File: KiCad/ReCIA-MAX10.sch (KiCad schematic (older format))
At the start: 30 parts, among them J1 Conn_02x03_Odd_Even, U1 AMS1117-3.3, U2 SN74CBT16210, U3 SN74CBT16210, U4 10M02SCU169, U5 8520_DIP_SOCKET, X1 Oscillator_3.2x2.5mm-28.6363M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

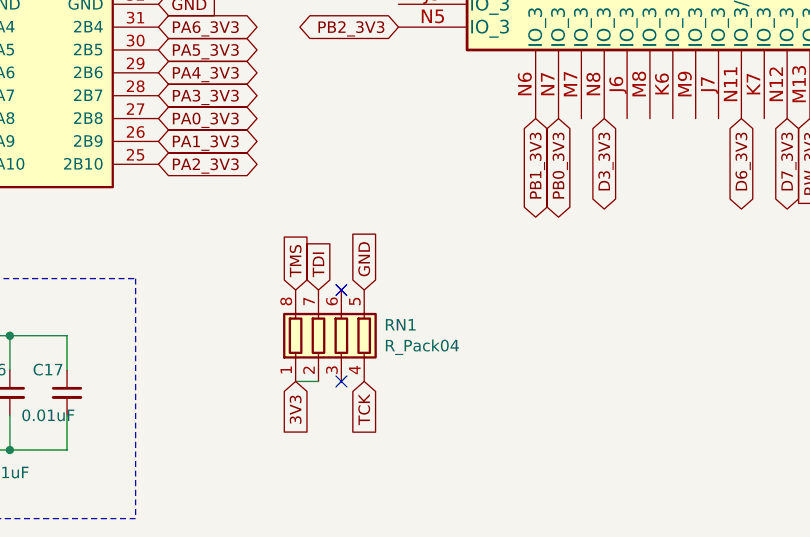
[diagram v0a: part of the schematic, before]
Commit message: Add 10k resistor pack RN2 with pull-ups for CONF_DONE, nSTATUS, nCONFIG
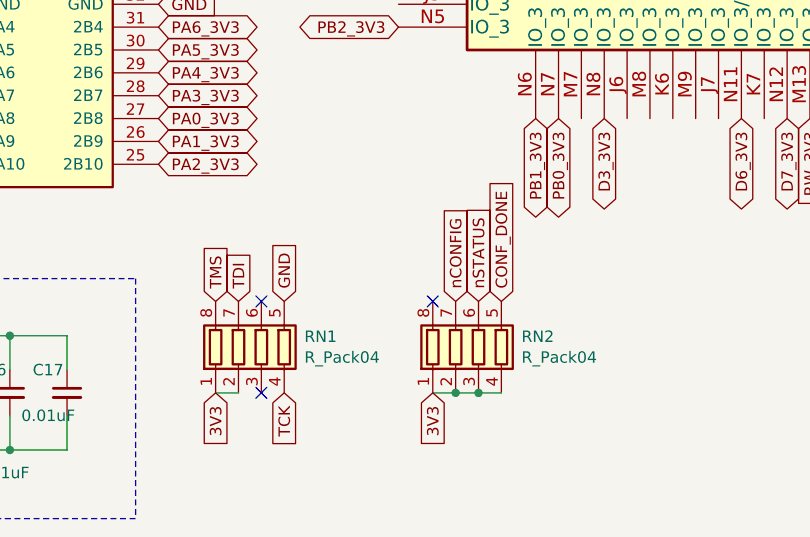
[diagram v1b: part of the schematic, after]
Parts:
- added RN2: R_Pack04, ReCIA:RESCAF80P320X160X60-8N, symbol Device:R_Pack04
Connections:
- net 3V3: now also RN2.1 (R1.1), RN2.2 (R2.1), RN2.3 (R3.1), RN2.4 (R4.1)
- net CONF_DONE: now also RN2.5 (R4.2)
- net nCONFIG: now also RN2.7 (R2.2)
- net nSTATUS: now also RN2.6 (R3.2)
- no-connect marks 4 -> 5
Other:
- moved on the sheet: RN1
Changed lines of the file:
@@
 L Device:R_Pack04 RN1
 U 1 1 672BF603
-P 5500 6900
-F 0 "RN1" H 5688 6946 50  0000 L CNN
-F 1 "R_Pack04" H 5688 6855 50  0000 L CNN
-F 2 "ReCIA:RESCAF80P320X160X60-8N" V 5775 6900 50  0001 C CNN
-F 3 "~" H 5500 6900 50  0001 C CNN
-	1    5500 6900
+P 5150 6950
+F 0 "RN1" H 5338 6996 50  0000 L CNN
+F 1 "R_Pack04" H 5338 6905 50  0000 L CNN
+F 2 "ReCIA:RESCAF80P320X160X60-8N" V 5425 6950 50  0001 C CNN
+F 3 "~" H 5150 6950 50  0001 C CNN
+	1    5150 6950
 	1    0    0    -1
 $EndComp
-Text GLabel 5600 6700 1    50   Input ~ 0
+Text GLabel 5250 6750 1    50   Input ~ 0
 GND
-Text GLabel 5600 7100 3    50   Input ~ 0
+Text GLabel 5250 7150 3    50   Input ~ 0
 TCK
-Text GLabel 5300 7100 3    50   Input ~ 0
+Text GLabel 4950 7150 3    50   Input ~ 0
 3V3
 Wire Wire Line
-	5300 7100 5400 7100
-Text GLabel 5300 6700 1    50   Input ~ 0
+	4950 7150 5050 7150
+Text GLabel 4950 6750 1    50   Input ~ 0
 TMS
-Text GLabel 5400 6700 1    50   Input ~ 0
+Text GLabel 5050 6750 1    50   Input ~ 0
 TDI
-NoConn ~ 5500 6700
-NoConn ~ 5500 7100
+NoConn ~ 5150 6750
+NoConn ~ 5150 7150
+$Comp
+L Device:R_Pack04 RN2
+U 1 1 67322D49
+P 6100 6950
+F 0 "RN2" H 6288 6996 50  0000 L CNN
+F 1 "R_Pack04" H 6288 6905 50  0000 L CNN
+F 2 "ReCIA:RESCAF80P320X160X60-8N" V 6375 6950 50  0001 C CNN
+F 3 "~" H 6100 6950 50  0001 C CNN
+	1    6100 6950
+	1    0    0    -1
+$EndComp
+Text GLabel 6200 6750 1    50   Input ~ 0
+CONF_DONE
+Text GLabel 6100 6750 1    50   Input ~ 0
+nSTATUS
+Text GLabel 6000 6750 1    50   Input ~ 0
+nCONFIG
+Text GLabel 5900 7150 3    50   Input ~ 0
+3V3
+Wire Wire Line
+	5900 7150 6000 7150
+Connection ~ 6000 7150
+Wire Wire Line
+	6000 7150 6100 7150
+Wire Wire Line
+	6100 7150 6200 7150
+Connection ~ 6100 7150
+NoConn ~ 5900 6750
 $EndSCHEMATC

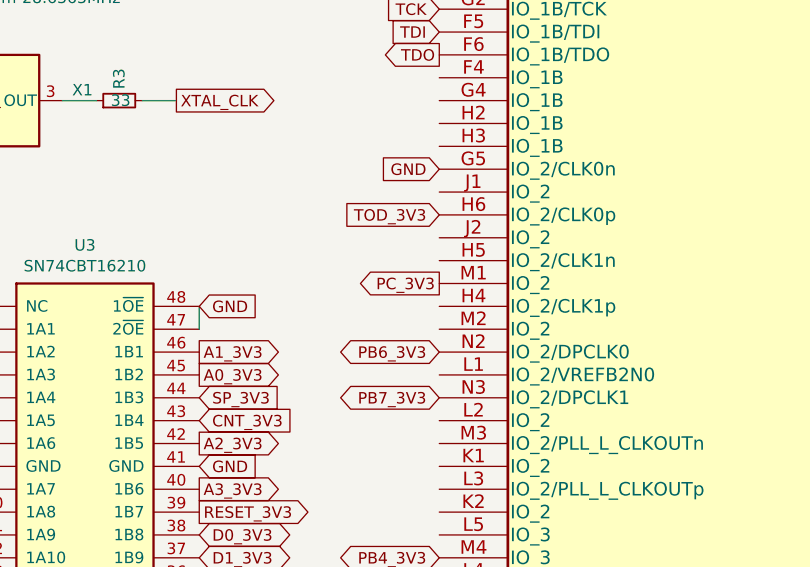
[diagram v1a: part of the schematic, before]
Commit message: Assign H4,H5 pad to GND
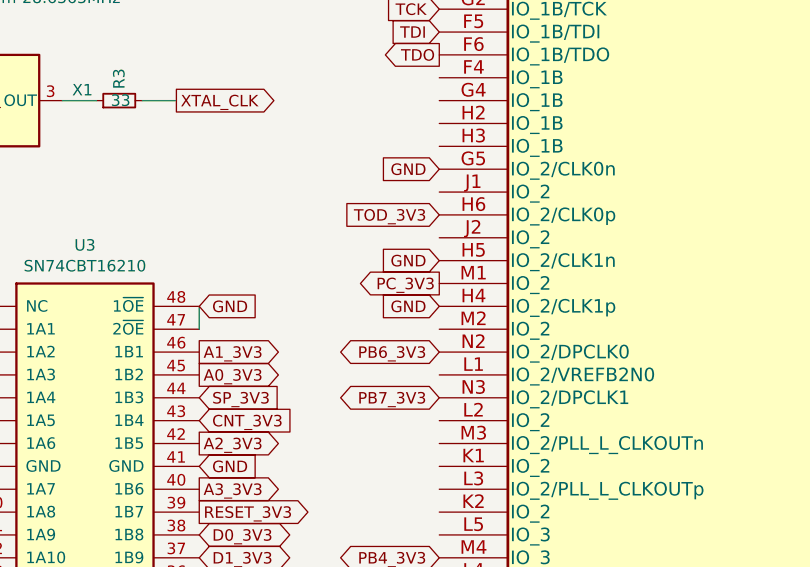
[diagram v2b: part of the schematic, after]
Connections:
- net GND: now also U4.H4 (IO_2/CLK1p), U4.H5 (IO_2/CLK1n)
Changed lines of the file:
@@
 Connection ~ 6100 7150
 NoConn ~ 5900 6750
+Text GLabel 5750 3650 0    50   Input ~ 0
+GND
+Text GLabel 5750 3850 0    50   Input ~ 0
+GND
 $EndSCHEMATC
